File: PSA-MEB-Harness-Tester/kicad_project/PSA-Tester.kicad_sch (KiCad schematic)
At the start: 37 parts, among them J11 TYPE-C-31-M-04, SW1 B3FS-1010P, SW2 B3FS-1010P, SW3 B3FS-1010P, U1 MCP23017T-E/SO, U10 ESP32-C3-OLED, U2 MCP23017T-E/SO, U3 MCP23017T-E/SO, U4 MCP23017T-E/SO, U5 MCP23017T-E/SO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

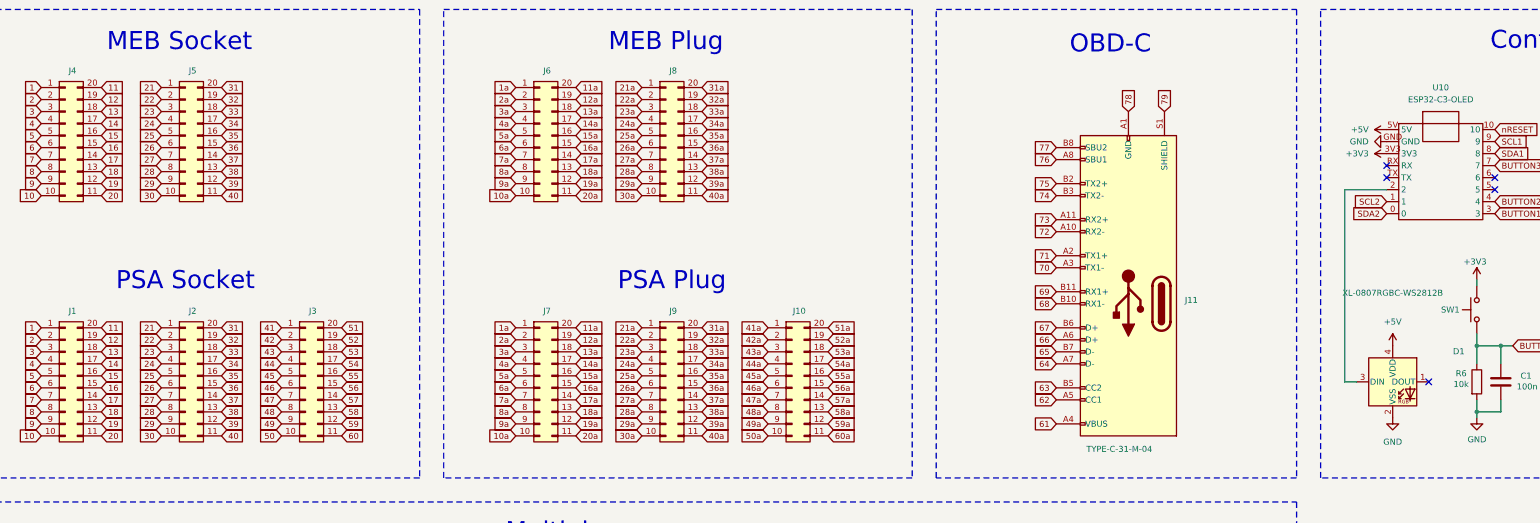
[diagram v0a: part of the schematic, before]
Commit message: fix PSA-Tester swapped pin headers
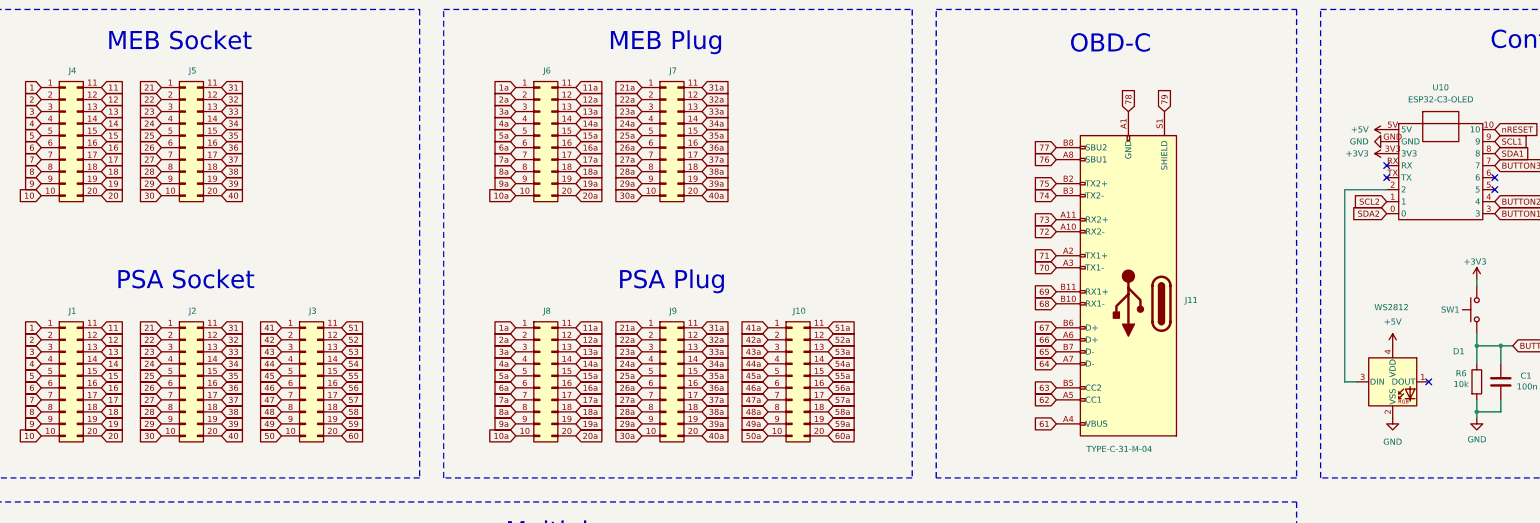
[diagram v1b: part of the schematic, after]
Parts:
- D1: value XL-0807RGBC-WS2812B -> WS2812; footprint 0_tester:LED_WS2812B-2020_PLCC4_2.0x2.0mm -> LED_SMD:LED_WS2812B_PLCC4_5.0x5.0mm_P3.2mm
- J1, J10, J2, J3, J4, J5, J6, J9: footprint Connector_PinHeader_2.54mm:PinHeader_2x10_P2.54mm_Vertical -> 0_tester:PinHeader_2x10_P2.54mm_Vertical; symbol Connector_Generic:Conn_02x10_Counter_Clockwise -> Connector_Generic:Conn_02x10_Top_Bottom
- J7: renamed from J8; footprint Connector_PinHeader_2.54mm:PinHeader_2x10_P2.54mm_Vertical -> 0_tester:PinHeader_2x10_P2.54mm_Vertical; symbol Connector_Generic:Conn_02x10_Counter_Clockwise -> Connector_Generic:Conn_02x10_Top_Bottom
- J8: renamed from J7; footprint Connector_PinHeader_2.54mm:PinHeader_2x10_P2.54mm_Vertical -> 0_tester:PinHeader_2x10_P2.54mm_Vertical; symbol Connector_Generic:Conn_02x10_Counter_Clockwise -> Connector_Generic:Conn_02x10_Top_Bottom
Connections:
- net 11: now also J1.11 (Pin_11), J4.11 (Pin_11); no longer J1.20 (Pin_20), J4.20 (Pin_20)
- net 11a: now also J6.11 (Pin_11), J8.11 (Pin_11); no longer J6.20 (Pin_20), J8.20 (Pin_20)
- net 12: now also J1.12 (Pin_12), J4.12 (Pin_12); no longer J1.19 (Pin_19), J4.19 (Pin_19)
- net 12a: now also J6.12 (Pin_12), J8.12 (Pin_12); no longer J6.19 (Pin_19), J8.19 (Pin_19)
- net 13: now also J1.13 (Pin_13), J4.13 (Pin_13); no longer J1.18 (Pin_18), J4.18 (Pin_18)
- net 13a: now also J6.13 (Pin_13), J8.13 (Pin_13); no longer J6.18 (Pin_18), J8.18 (Pin_18)
- net 14: now also J1.14 (Pin_14), J4.14 (Pin_14); no longer J1.17 (Pin_17), J4.17 (Pin_17)
- net 14a: now also J6.14 (Pin_14), J8.14 (Pin_14); no longer J6.17 (Pin_17), J8.17 (Pin_17)
- net 15: now also J1.15 (Pin_15), J4.15 (Pin_15); no longer J1.16 (Pin_16), J4.16 (Pin_16)
- net 15a: now also J6.15 (Pin_15), J8.15 (Pin_15); no longer J6.16 (Pin_16), J8.16 (Pin_16)
- net 16: now also J1.16 (Pin_16), J4.16 (Pin_16); no longer J1.15 (Pin_15), J4.15 (Pin_15)
- net 16a: now also J6.16 (Pin_16), J8.16 (Pin_16); no longer J6.15 (Pin_15), J8.15 (Pin_15)
- net 17: now also J1.17 (Pin_17), J4.17 (Pin_17); no longer J1.14 (Pin_14), J4.14 (Pin_14)
- net 17a: now also J6.17 (Pin_17), J8.17 (Pin_17); no longer J6.14 (Pin_14), J8.14 (Pin_14)
- net 18: now also J1.18 (Pin_18), J4.18 (Pin_18); no longer J1.13 (Pin_13), J4.13 (Pin_13)
- net 18a: now also J6.18 (Pin_18), J8.18 (Pin_18); no longer J6.13 (Pin_13), J8.13 (Pin_13)
- net 19: now also J1.19 (Pin_19), J4.19 (Pin_19); no longer J1.12 (Pin_12), J4.12 (Pin_12)
- net 19a: now also J6.19 (Pin_19), J8.19 (Pin_19); no longer J6.12 (Pin_12), J8.12 (Pin_12)
- net 20: now also J1.20 (Pin_20), J4.20 (Pin_20); no longer J1.11 (Pin_11), J4.11 (Pin_11)
- net 20a: now also J6.20 (Pin_20), J8.20 (Pin_20); no longer J6.11 (Pin_11), J8.11 (Pin_11)
- net 31: now also J2.11 (Pin_11), J5.11 (Pin_11); no longer J2.20 (Pin_20), J5.20 (Pin_20)
- net 31a: now also J7.11 (Pin_11), J9.11 (Pin_11); no longer J7.20 (Pin_20), J9.20 (Pin_20)
- net 32: now also J2.12 (Pin_12), J5.12 (Pin_12); no longer J2.19 (Pin_19), J5.19 (Pin_19)
- net 32a: now also J7.12 (Pin_12), J9.12 (Pin_12); no longer J7.19 (Pin_19), J9.19 (Pin_19)
- net 33: now also J2.13 (Pin_13), J5.13 (Pin_13); no longer J2.18 (Pin_18), J5.18 (Pin_18)
- net 33a: now also J7.13 (Pin_13), J9.13 (Pin_13); no longer J7.18 (Pin_18), J9.18 (Pin_18)
- net 34: now also J2.14 (Pin_14), J5.14 (Pin_14); no longer J2.17 (Pin_17), J5.17 (Pin_17)
- net 34a: now also J7.14 (Pin_14), J9.14 (Pin_14); no longer J7.17 (Pin_17), J9.17 (Pin_17)
- net 35: now also J2.15 (Pin_15), J5.15 (Pin_15); no longer J2.16 (Pin_16), J5.16 (Pin_16)
- net 35a: now also J7.15 (Pin_15), J9.15 (Pin_15); no longer J7.16 (Pin_16), J9.16 (Pin_16)
- net 36: now also J2.16 (Pin_16), J5.16 (Pin_16); no longer J2.15 (Pin_15), J5.15 (Pin_15)
- net 36a: now also J7.16 (Pin_16), J9.16 (Pin_16); no longer J7.15 (Pin_15), J9.15 (Pin_15)
- net 37: now also J2.17 (Pin_17), J5.17 (Pin_17); no longer J2.14 (Pin_14), J5.14 (Pin_14)
- net 37a: now also J7.17 (Pin_17), J9.17 (Pin_17); no longer J7.14 (Pin_14), J9.14 (Pin_14)
- net 38: now also J2.18 (Pin_18), J5.18 (Pin_18); no longer J2.13 (Pin_13), J5.13 (Pin_13)
- net 38a: now also J7.18 (Pin_18), J9.18 (Pin_18); no longer J7.13 (Pin_13), J9.13 (Pin_13)
- net 39: now also J2.19 (Pin_19), J5.19 (Pin_19); no longer J2.12 (Pin_12), J5.12 (Pin_12)
- net 39a: now also J7.19 (Pin_19), J9.19 (Pin_19); no longer J7.12 (Pin_12), J9.12 (Pin_12)
- net 40: now also J2.20 (Pin_20), J5.20 (Pin_20); no longer J2.11 (Pin_11), J5.11 (Pin_11)
- net 40a: now also J7.20 (Pin_20), J9.20 (Pin_20); no longer J7.11 (Pin_11), J9.11 (Pin_11)
- net 51: now also J3.11 (Pin_11); no longer J3.20 (Pin_20)
- net 51a: now also J10.11 (Pin_11); no longer J10.20 (Pin_20)
- net 52: now also J3.12 (Pin_12); no longer J3.19 (Pin_19)
- net 52a: now also J10.12 (Pin_12); no longer J10.19 (Pin_19)
- net 53: now also J3.13 (Pin_13); no longer J3.18 (Pin_18)
- net 53a: now also J10.13 (Pin_13); no longer J10.18 (Pin_18)
- net 54: now also J3.14 (Pin_14); no longer J3.17 (Pin_17)
- net 54a: now also J10.14 (Pin_14); no longer J10.17 (Pin_17)
- net 55: now also J3.15 (Pin_15); no longer J3.16 (Pin_16)
- net 55a: now also J10.15 (Pin_15); no longer J10.16 (Pin_16)
- net 56: now also J3.16 (Pin_16); no longer J3.15 (Pin_15)
- net 56a: now also J10.16 (Pin_16); no longer J10.15 (Pin_15)
- net 57: now also J3.17 (Pin_17); no longer J3.14 (Pin_14)
- net 57a: now also J10.17 (Pin_17); no longer J10.14 (Pin_14)
- net 58: now also J3.18 (Pin_18); no longer J3.13 (Pin_13)
- net 58a: now also J10.18 (Pin_18); no longer J10.13 (Pin_13)
- net 59: now also J3.19 (Pin_19); no longer J3.12 (Pin_12)
- net 59a: now also J10.19 (Pin_19); no longer J10.12 (Pin_12)
- net 60: now also J3.20 (Pin_20); no longer J3.11 (Pin_11)
- net 60a: now also J10.20 (Pin_20); no longer J10.11 (Pin_11)
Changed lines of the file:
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@@
 			)
 		)
-		(property "Value" "XL-0807RGBC-WS2812B"
-			(at 318.77 77.724 0)
+		(property "Value" "WS2812"
+			(at 318.516 80.772 0)
 			(effects
 				(font
@@
 			)
 		)
-		(property "Footprint" "0_tester:LED_WS2812B-2020_PLCC4_2.0x2.0mm"
+		(property "Footprint" "LED_SMD:LED_WS2812B_PLCC4_5.0x5.0mm_P3.2mm"
 			(at 320.04 104.14 0)
 			(effects
@@
 	)
 	(symbol
-		(lib_id "Connector_Generic:Conn_02x10_Counter_Clockwise")
+		(lib_id "Connector_Generic:Conn_02x10_Top_Bottom")
 		(at 38.1 95.25 0)
 		(unit 1)
@@
 			)
 		)
-		(property "Footprint" "Connector_PinHeader_2.54mm:PinHeader_2x10_P2.54mm_Vertical"
+		(property "Footprint" "0_tester:PinHeader_2x10_P2.54mm_Vertical"
 			(at 38.1 95.25 0)
 			(effects
@@
 			)
 		)
-		(property "Description" "Generic connector, double row, 02x10, counter clockwise pin numbering scheme (similar to DIP package numbering), script generated (kicad-library-utils/schlib/autogen/connector/)"
+		(property "Description" "Generic connector, double row, 02x10, top/bottom pin numbering scheme (row 1: 1...pins_per_row, row2: pins_per_row+1 ... num_pins), script generated (kicad-library-utils/schlib/autogen/connector/)"
 			(at 38.1 95.25 0)
 			(effects
@@
 	)
 	(symbol
-		(lib_id "Connector_Generic:Conn_02x10_Counter_Clockwise")
+		(lib_id "Connector_Generic:Conn_02x10_Top_Bottom")
 		(at 138.43 95.25 0)
 		(unit 1)
@@
 		(on_board yes)
 		(dnp no)
-		(property "Reference" "J7"
+		(property "Reference" "J8"
 			(at 139.954 81.534 0)
 			(effects
@@
 			)
 		)
-		(property "Footprint" "Connector_PinHeader_2.54mm:PinHeader_2x10_P2.54mm_Vertical"
+		(property "Footprint" "0_tester:PinHeader_2x10_P2.54mm_Vertical"
 			(at 138.43 95.25 0)
 			(effects
@@
 			)
 		)
-		(property "Description" "Generic connector, double row, 02x10, counter clockwise pin numbering scheme (similar to DIP package numbering), script generated (kicad-library-utils/schlib/autogen/connector/)"
+		(property "Description" "Generic connector, double row, 02x10, top/bottom pin numbering scheme (row 1: 1...pins_per_row, row2: pins_per_row+1 ... num_pins), script generated (kicad-library-utils/schlib/autogen/connector/)"
 			(at 138.43 95.25 0)
 			(effects
@@
 			(project "PSA-Tester"
 				(path "/e0029412-f2c0-4791-9162-eded45ef3b03"
-					(reference "J7")
+					(reference "J8")
 					(unit 1)
 				)
@@
 	)
 	(symbol
-		(lib_id "Connector_Generic:Conn_02x10_Counter_Clockwise")
+		(lib_id "Connector_Generic:Conn_02x10_Top_Bottom")
 		(at 63.5 95.25 0)
 		(unit 1)
@@
 			)
 		)
-		(property "Footprint" "Connector_PinHeader_2.54mm:PinHeader_2x10_P2.54mm_Vertical"
+		(property "Footprint" "0_tester:PinHeader_2x10_P2.54mm_Vertical"
 			(at 63.5 95.25 0)
 			(effects
@@
 			)
 		)
-		(property "Description" "Generic connector, double row, 02x10, counter clockwise pin numbering scheme (similar to DIP package numbering), script generated (kicad-library-utils/schlib/autogen/connector/)"
+		(property "Description" "Generic connector, double row, 02x10, top/bottom pin numbering scheme (row 1: 1...pins_per_row, row2: pins_per_row+1 ... num_pins), script generated (kicad-library-utils/schlib/autogen/connector/)"
 			(at 63.5 95.25 0)
 			(effects
@@
 	)
 	(symbol
-		(lib_id "Connector_Generic:Conn_02x10_Counter_Clockwise")
+		(lib_id "Connector_Generic:Conn_02x10_Top_Bottom")
 		(at 38.1 44.45 0)
 		(unit 1)
@@
 			)
 		)
-		(property "Footprint" "Connector_PinHeader_2.54mm:PinHeader_2x10_P2.54mm_Vertical"
+		(property "Footprint" "0_tester:PinHeader_2x10_P2.54mm_Vertical"
 			(at 38.1 44.45 0)
 			(effects
@@
 			)
 		)
-		(property "Description" "Generic connector, double row, 02x10, counter clockwise pin numbering scheme (similar to DIP package numbering), script generated (kicad-library-utils/schlib/autogen/connector/)"
+		(property "Description" "Generic connector, double row, 02x10, top/bottom pin numbering scheme (row 1: 1...pins_per_row, row2: pins_per_row+1 ... num_pins), script generated (kicad-library-utils/schlib/autogen/connector/)"
 			(at 38.1 44.45 0)
 			(effects
@@
 	)
 	(symbol
-		(lib_id "Connector_Generic:Conn_02x10_Counter_Clockwise")
+		(lib_id "Connector_Generic:Conn_02x10_Top_Bottom")
 		(at 88.9 95.25 0)
 		(unit 1)
@@
 			)
 		)
-		(property "Footprint" "Connector_PinHeader_2.54mm:PinHeader_2x10_P2.54mm_Vertical"
+		(property "Footprint" "0_tester:PinHeader_2x10_P2.54mm_Vertical"
 			(at 88.9 95.25 0)
 			(effects
@@
 			)
 		)
-		(property "Description" "Generic connector, double row, 02x10, counter clockwise pin numbering scheme (similar to DIP package numbering), script generated (kicad-library-utils/schlib/autogen/connector/)"
+		(property "Description" "Generic connector, double row, 02x10, top/bottom pin numbering scheme (row 1: 1...pins_per_row, row2: pins_per_row+1 ... num_pins), script generated (kicad-library-utils/schlib/autogen/connector/)"
 			(at 88.9 95.25 0)
 			(effects
@@
 	)
 	(symbol
-		(lib_id "Connector_Generic:Conn_02x10_Counter_Clockwise")
+		(lib_id "Connector_Generic:Conn_02x10_Top_Bottom")
 		(at 191.77 95.25 0)
 		(unit 1)
@@
 			)
 		)
-		(property "Footprint" "Connector_PinHeader_2.54mm:PinHeader_2x10_P2.54mm_Vertical"
+		(property "Footprint" "0_tester:PinHeader_2x10_P2.54mm_Vertical"
 			(at 191.77 95.25 0)
 			(effects
@@
 			)
 		)
-		(property "Description" "Generic connector, double row, 02x10, counter clockwise pin numbering scheme (similar to DIP package numbering), script generated (kicad-library-utils/schlib/autogen/connector/)"
+		(property "Description" "Generic connector, double row, 02x10, top/bottom pin numbering scheme (row 1: 1...pins_per_row, row2: pins_per_row+1 ... num_pins), script generated (kicad-library-utils/schlib/autogen/connector/)"
 			(at 191.77 95.25 0)
 			(effects
@@
 	)
 	(symbol
-		(lib_id "Connector_Generic:Conn_02x10_Counter_Clockwise")
+		(lib_id "Connector_Generic:Conn_02x10_Top_Bottom")
 		(at 63.5 44.45 0)
 		(unit 1)
@@
 			)
 		)
-		(property "Footprint" "Connector_PinHeader_2.54mm:PinHeader_2x10_P2.54mm_Vertical"
+		(property "Footprint" "0_tester:PinHeader_2x10_P2.54mm_Vertical"
 			(at 63.5 44.45 0)
 			(effects
@@
 			)
 		)
-		(property "Description" "Generic connector, double row, 02x10, counter clockwise pin numbering scheme (similar to DIP package numbering), script generated (kicad-library-utils/schlib/autogen/connector/)"
+		(property "Description" "Generic connector, double row, 02x10, top/bottom pin numbering scheme (row 1: 1...pins_per_row, row2: pins_per_row+1 ... num_pins), script generated (kicad-library-utils/schlib/autogen/connector/)"
 			(at 63.5 44.45 0)
 			(effects
@@
 	)
 	(symbol
-		(lib_id "Connector_Generic:Conn_02x10_Counter_Clockwise")
+		(lib_id "Connector_Generic:Conn_02x10_Top_Bottom")
 		(at 165.1 44.45 0)
 		(unit 1)
@@
 		(on_board yes)
 		(dnp no)
-		(property "Reference" "J8"
+		(property "Reference" "J7"
 			(at 166.624 30.734 0)
 			(effects
@@
 			)
 		)
-		(property "Footprint" "Connector_PinHeader_2.54mm:PinHeader_2x10_P2.54mm_Vertical"
+		(property "Footprint" "0_tester:PinHeader_2x10_P2.54mm_Vertical"
 			(at 165.1 44.45 0)
 			(effects
@@
 			)
 		)
-		(property "Description" "Generic connector, double row, 02x10, counter clockwise pin numbering scheme (similar to DIP package numbering), script generated (kicad-library-utils/schlib/autogen/connector/)"
+		(property "Description" "Generic connector, double row, 02x10, top/bottom pin numbering scheme (row 1: 1...pins_per_row, row2: pins_per_row+1 ... num_pins), script generated (kicad-library-utils/schlib/autogen/connector/)"
 			(at 165.1 44.45 0)
 			(effects
@@
 			(project "PSA-Tester"
 				(path "/e0029412-f2c0-4791-9162-eded45ef3b03"
-					(reference "J8")
+					(reference "J7")
 					(unit 1)
 				)
@@
 	)
 	(symbol
-		(lib_id "Connector_Generic:Conn_02x10_Counter_Clockwise")
+		(lib_id "Connector_Generic:Conn_02x10_Top_Bottom")
 		(at 165.1 95.25 0)
 		(unit 1)
@@
 			)
 		)
-		(property "Footprint" "Connector_PinHeader_2.54mm:PinHeader_2x10_P2.54mm_Vertical"
+		(property "Footprint" "0_tester:PinHeader_2x10_P2.54mm_Vertical"
 			(at 165.1 95.25 0)
 			(effects
@@
 			)
 		)
-		(property "Description" "Generic connector, double row, 02x10, counter clockwise pin numbering scheme (similar to DIP package numbering), script generated (kicad-library-utils/schlib/autogen/connector/)"
+		(property "Description" "Generic connector, double row, 02x10, top/bottom pin numbering scheme (row 1: 1...pins_per_row, row2: pins_per_row+1 ... num_pins), script generated (kicad-library-utils/schlib/autogen/connector/)"
 			(at 165.1 95.25 0)
 			(effects
@@
 	)
 	(symbol
-		(lib_id "Connector_Generic:Conn_02x10_Counter_Clockwise")
+		(lib_id "Connector_Generic:Conn_02x10_Top_Bottom")
 		(at 138.43 44.45 0)
 		(unit 1)
@@
 			)
 		)
-		(property "Footprint" "Connector_PinHeader_2.54mm:PinHeader_2x10_P2.54mm_Vertical"
+		(property "Footprint" "0_tester:PinHeader_2x10_P2.54mm_Vertical"
 			(at 138.43 44.45 0)
 			(effects
@@
 			)
 		)
-		(property "Description" "Generic connector, double row, 02x10, counter clockwise pin numbering scheme (similar to DIP package numbering), script generated (kicad-library-utils/schlib/autogen/connector/)"
+		(property "Description" "Generic connector, double row, 02x10, top/bottom pin numbering scheme (row 1: 1...pins_per_row, row2: pins_per_row+1 ... num_pins), script generated (kicad-library-utils/schlib/autogen/connector/)"
 			(at 138.43 44.45 0)
 			(effects

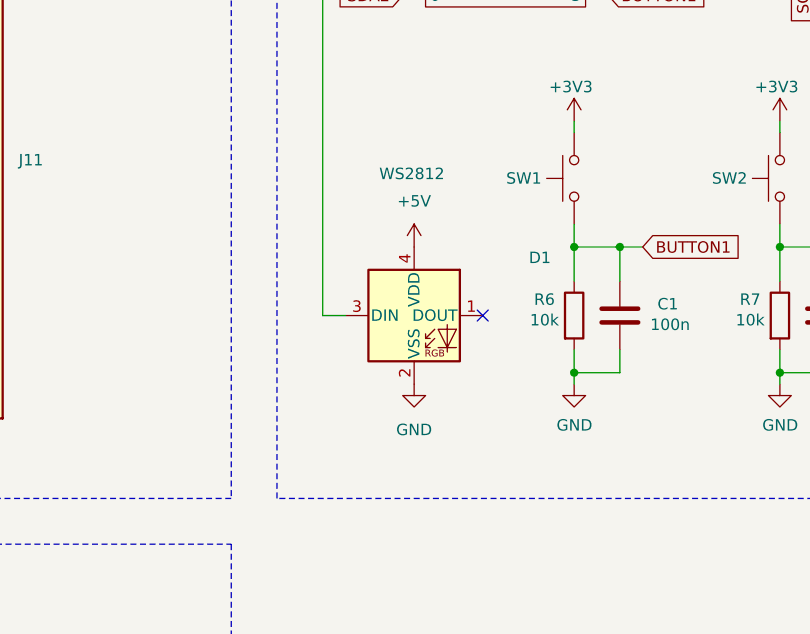
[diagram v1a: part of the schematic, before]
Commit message: swap switches, move sockets 4mm right
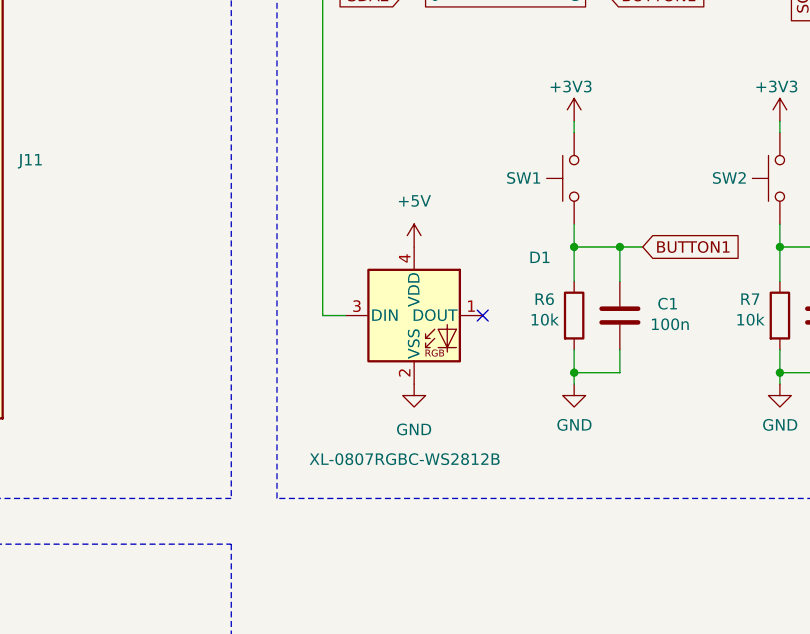
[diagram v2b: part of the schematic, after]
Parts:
- D1: value WS2812 -> XL-0807RGBC-WS2812B; footprint LED_SMD:LED_WS2812B_PLCC4_5.0x5.0mm_P3.2mm -> 0_tester:LED_WS2812B-2020_PLCC4_2.0x2.0mm
- SW1, SW2, SW3: value B3FS-1010P -> TS-1057S-03126
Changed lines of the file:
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@@
 			)
 		)
-		(property "Value" "WS2812"
-			(at 318.516 80.772 0)
+		(property "Value" "XL-0807RGBC-WS2812B"
+			(at 317.754 112.522 0)
 			(effects
 				(font
@@
 			)
 		)
-		(property "Footprint" "LED_SMD:LED_WS2812B_PLCC4_5.0x5.0mm_P3.2mm"
+		(property "Footprint" "0_tester:LED_WS2812B-2020_PLCC4_2.0x2.0mm"
 			(at 320.04 104.14 0)
 			(effects
@@
 			)
 		)
-		(property "Value" "B3FS-1010P"
+		(property "Value" "TS-1057S-03126"
 			(at 332.232 81.28 0)
 			(effects
@@
 			)
 		)
-		(property "Value" "B3FS-1010P"
+		(property "Value" "TS-1057S-03126"
 			(at 377.952 81.28 0)
 			(effects
@@
 			)
 		)
-		(property "Value" "B3FS-1010P"
+		(property "Value" "TS-1057S-03126"
 			(at 355.092 81.28 0)
 			(effects
